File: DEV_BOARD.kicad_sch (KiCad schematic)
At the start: 1 part, among them U1 MSPM0G350x

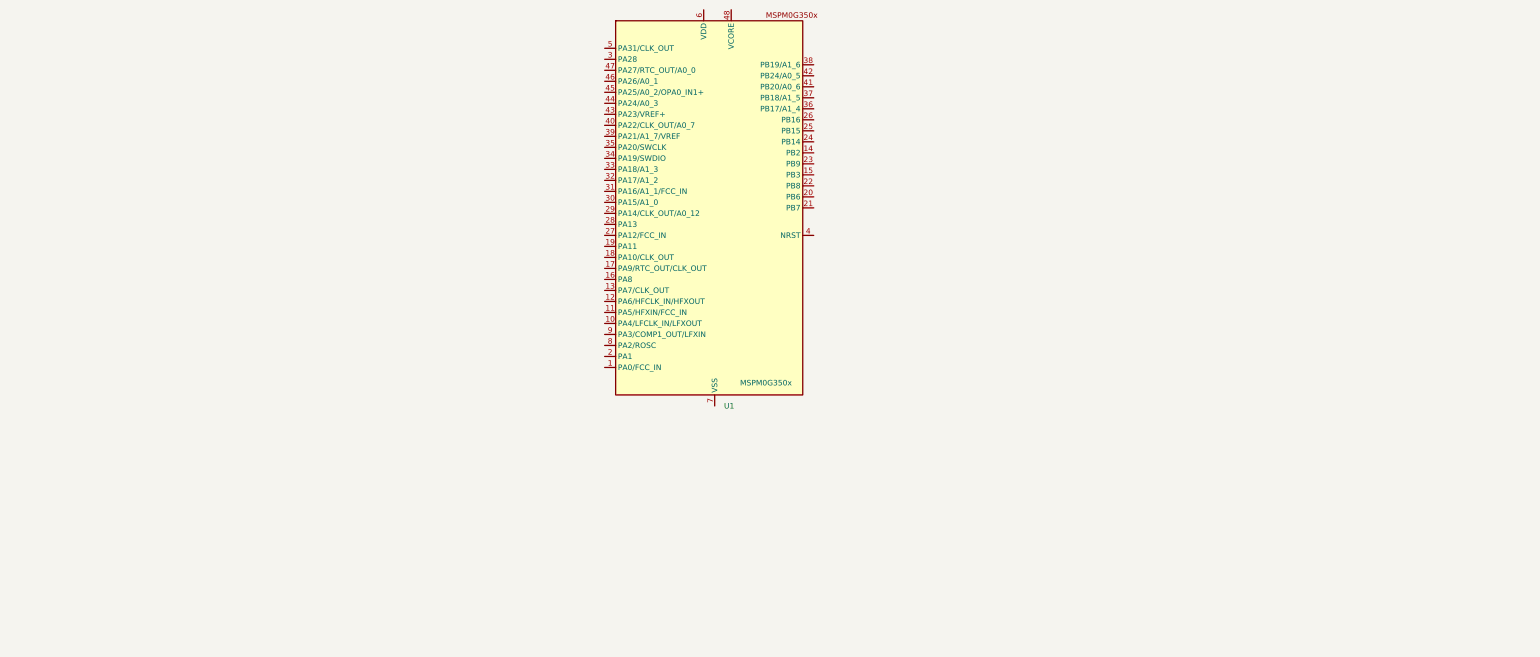
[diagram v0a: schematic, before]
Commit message: Part 2: Building the Core MCU Circuit
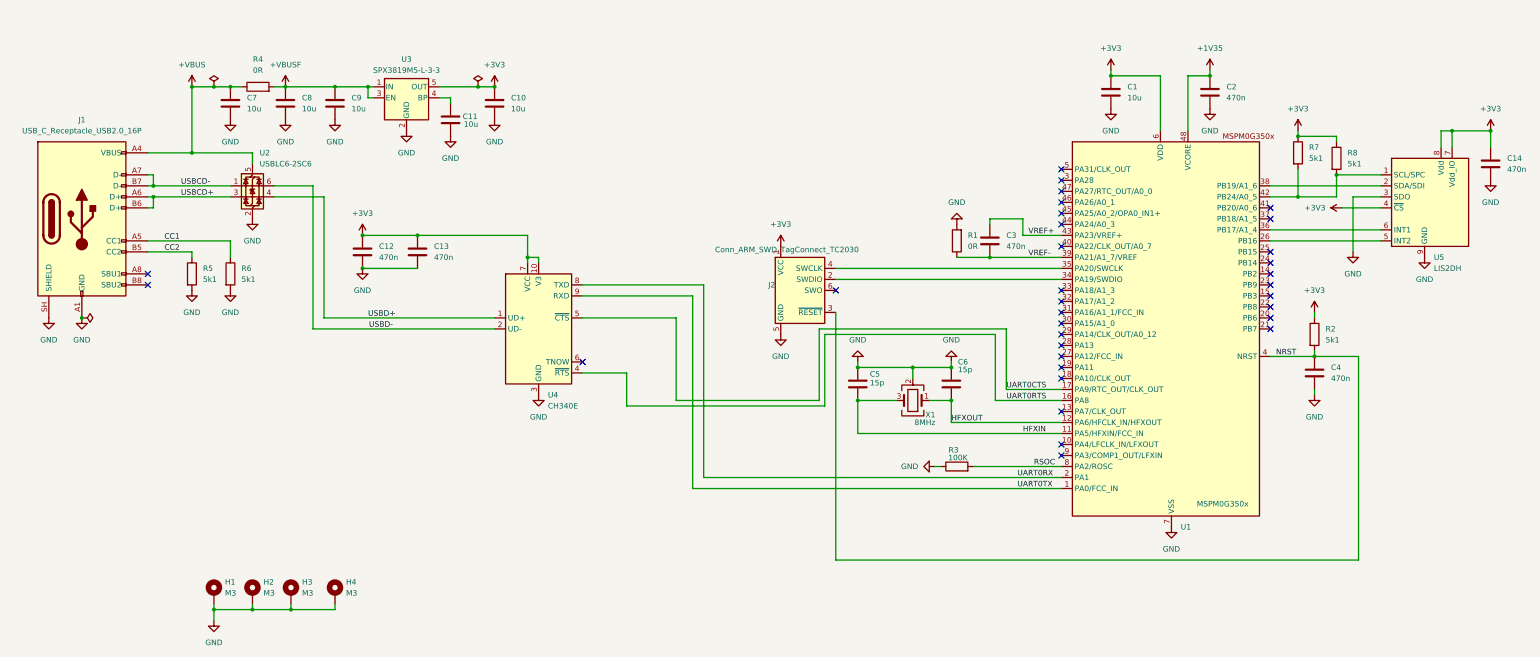
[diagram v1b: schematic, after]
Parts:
- added C1, C10, C11, C7, C8, C9: 10u, Capacitor_SMD:C_0805_2012Metric, symbol Device:C
- added C12, C13, C14, C2, C3, C4: 470n, Capacitor_SMD:C_0805_2012Metric, symbol Device:C
- added C5, C6: 15p, Capacitor_SMD:C_0805_2012Metric, symbol Device:C
- added H1, H2, H3, H4: M3, MountingHole:MountingHole_3.5mm_Pad_TopOnly, symbol Mechanical:MountingHole_Pad
- added J1: USB_C_Receptacle_USB2.0_16P, Connector_USB:USB_C_Receptacle_GCT_USB4105-xx-A_16P_TopMnt_Horizontal, symbol Connector:USB_C_Receptacle_USB2.0_16P
- added J2: Conn_ARM_SWD_TagConnect_TC2030, Connector:Tag-Connect_TC2030-IDC-FP_2x03_P1.27mm_Vertical, symbol Connector:Conn_ARM_SWD_TagConnect_TC2030
- added R1, R4: 0R, Resistor_SMD:R_0201_0603Metric, symbol Device:R
- added R2, R5, R6, R7, R8: 5k1, Resistor_SMD:R_0201_0603Metric, symbol Device:R
- added R3: 100K, Resistor_SMD:R_0201_0603Metric, symbol Device:R
- added U2: USBLC6-2SC6, Package_TO_SOT_SMD:SOT-23-6, symbol Power_Protection:USBLC6-2SC6
- added U3: SPX3819M5-L-3-3, Package_TO_SOT_SMD:SOT-23-5, symbol Regulator_Linear:SPX3819M5-L-3-3
- added U4: CH340E, Package_SO:MSOP-10_3x3mm_P0.5mm, symbol Interface_USB:CH340E
- added U5: LIS2DH, Package_LGA:LGA-14_2x2mm_P0.35mm_LayoutBorder3x4y, symbol Sensor_Motion:LIS2DH
- added X1: 8MHz, Crystal:Crystal_SMD_3225-4Pin_3.2x2.5mm, symbol Device:Crystal_GND24
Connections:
- net UART0TX: now reaches U1.1 (PA0/FCC_IN)
- net UART0TX: now also U4.9 (RXD)
- net HFXIN: now reaches U1.11 (PA5/HFXIN/FCC_IN)
- net HFXIN: now also C5.2, X1.3
- net HFXOUT: now reaches U1.12 (PA6/HFCLK_IN/HFXOUT)
- net HFXOUT: now also C6.2, X1.1
- net UART0RTS: now reaches U1.16 (PA8)
- net UART0RTS: now also U4.4 (~{RTS})
- net UART0CTS: now reaches U1.17 (PA9/RTC_OUT/CLK_OUT)
- net UART0CTS: now also U4.5 (~{CTS})
- net UART0RX: now reaches U1.2 (PA1)
- net UART0RX: now also U4.8 (TXD)
- net at U1.26 (PB16): now also U5.5 (INT2)
- net at U1.34 (PA19/SWDIO): now also J2.2 (SWDIO)
- net at U1.35 (PA20/SWCLK): now also J2.4 (SWCLK)
- net at U1.36 (PB17/A1_4): now also U5.6 (INT1)
- net at U1.38 (PB19/A1_6): now also U5.2 (SDA/SDI)
- net VREF-: now reaches U1.39 (PA21/A1_7/VREF)
- net VREF-: now also C3.2, R1.1
- net NRST: now reaches U1.4 (NRST)
- net NRST: now also C4.1, J2.3 (~{RESET}), R2.2
- net at U1.42 (PB24/A0_5): now also R7.2, R8.2, U5.1 (SCL/SPC)
- net VREF+: now reaches U1.43 (PA23/VREF+)
- net VREF+: now also C3.1
- net +1V35: now reaches U1.48 (VCORE)
- net +1V35: now also C2.1
- net +3V3: now reaches U1.6 (VDD)
- net +3V3: now also C1.1, C10.1, C12.1, C13.1, C14.1, J2.1 (VCC), R2.1, R7.1, R8.1, U3.5 (OUT), U4.10 (V3), U4.7 (VCC), U5.4 (~{CS}), U5.7 (Vdd_IO), U5.8 (Vdd)
- net GND: now reaches U1.7 (VSS)
- net GND: now also C1.2, C10.2, C11.2, C12.2, C13.2, C14.2, C2.2, C4.2, C5.1, C6.1, C7.2, C8.2, C9.2, H1.1, H2.1, H3.1, H4.1, J1.A1 (GND), J1.A12 (GND), J1.B1 (GND), J1.B12 (GND), J1.SH (SHIELD), J2.5 (GND), R1.2, R3.1, R5.2, R6.2, U2.2 (GND), U3.2 (GND), U4.3 (GND), U5.10 (GND), U5.11 (GND), U5.12 (GND), U5.13 (GND), U5.14 (GND), U5.3 (SDO), U5.9 (GND), X1.2 (G), X1.4 (G)
- net RSOC: now reaches U1.8 (PA2/ROSC)
- net RSOC: now also R3.2
- new net: C11.1, U3.4 (BP)
- new net +VBUS: C7.1, J1.A4 (VBUS), J1.A9 (VBUS), J1.B4 (VBUS), J1.B9 (VBUS), R4.1, U2.5 (VBUS)
- new net +VBUSF: C8.1, C9.1, R4.2, U3.1 (IN), U3.3 (EN)
- new net CC1: J1.A5 (CC1), R6.1
- new net CC2: J1.B5 (CC2), R5.1
- new net USBCD+: J1.A6 (D+), J1.B6 (D+), U2.3 (I/O2)
- new net USBCD-: J1.A7 (D-), J1.B7 (D-), U2.1 (I/O1)
- new net USBD+: U2.4 (I/O2), U4.1 (UD+)
- new net USBD-: U2.6 (I/O1), U4.2 (UD-)
- no-connect marks 0 -> 33
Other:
- moved on the sheet: U1
